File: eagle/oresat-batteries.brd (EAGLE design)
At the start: 94 x 93.5 mm, 73 parts, among them IC1 74AHC1G08DBV, U1 TCAN330, U2 STM32F042K6, U3 ADP5062, X1 16MHz

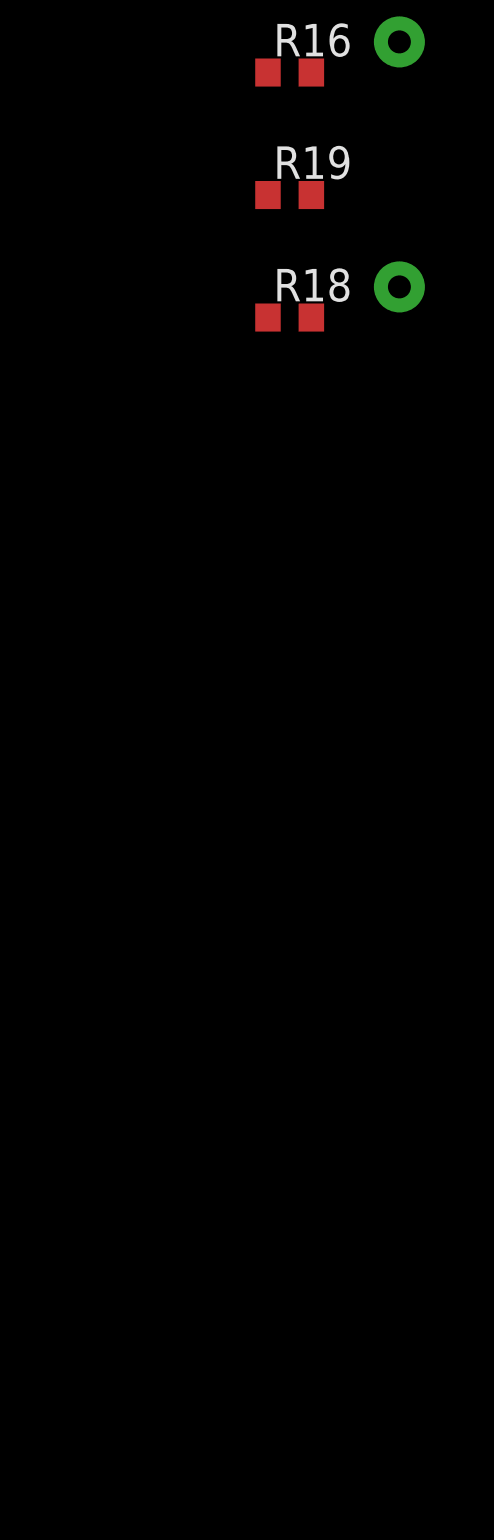
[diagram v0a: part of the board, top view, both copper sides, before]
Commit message: Added 3.3V switching power supply
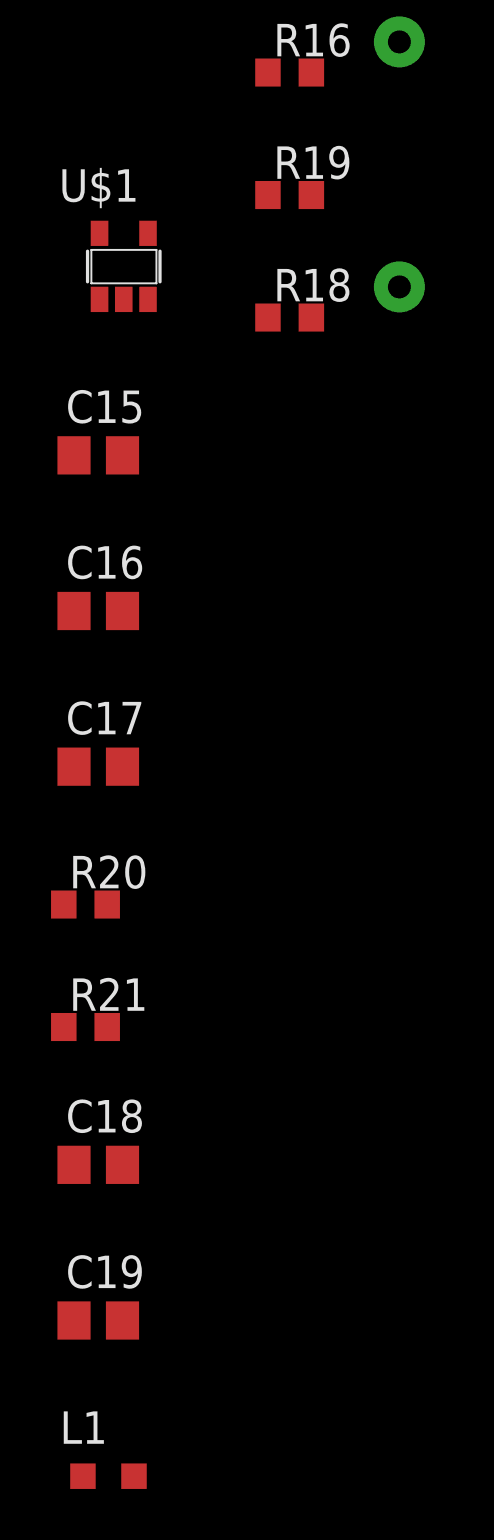
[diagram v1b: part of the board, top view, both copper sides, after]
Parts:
- added C15, C16, C17, C18, C19: 10u, rcl:C0805
- added L1: (no value), rcl:L2012C
- added R20, R21: 10k, rcl:R0603
- added U$1: LM3761, oresat-batteries:SOT23-5
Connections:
- new net N$1: L1.2, U$1.5
- new net N$3: C18.1, C19.1, L1.1, U$1.4
- new net N$7: C17.1, R20.2, R21.1, U$1.3
- net GND: now also C15.2, C16.2, C17.2, C18.2, C19.2, R20.1, U$1.2
- net VSOLAR: now also C15.1, C16.1, R21.2, U$1.1
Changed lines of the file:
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@@
 <element name="R19" library="rcl" package="R0603" value="DNP/10k" x="-21.4" y="-48.5"/>
 <element name="TP5" library="oresat-batteries" package="2MM_TP" value="TP" x="-17.1" y="-52.1"/>
+<element name="U$1" library="oresat-batteries" package="SOT23-5" value="LM3761" x="-27.9" y="-51.3"/>
+<element name="C15" library="rcl" package="C0805" value="10u" x="-28.9" y="-58.7"/>
+<element name="C16" library="rcl" package="C0805" value="10u" x="-28.9" y="-64.8"/>
+<element name="C17" library="rcl" package="C0805" value="10u" x="-28.9" y="-70.9"/>
+<element name="R20" library="rcl" package="R0603" value="10k" x="-29.4" y="-76.3"/>
+<element name="R21" library="rcl" package="R0603" value="10k" x="-29.4" y="-81.1"/>
+<element name="C18" library="rcl" package="C0805" value="10u" x="-28.9" y="-86.5"/>
+<element name="C19" library="rcl" package="C0805" value="10u" x="-28.9" y="-92.6"/>
+<element name="L1" library="rcl" package="L2012C" value="" x="-28.5" y="-98.7"/>
 </elements>
 <signals>
@@
 <contactref element="R17" pad="1"/>
 <contactref element="R19" pad="1"/>
-<wire x1="21.85" y1="80.08" x2="20.85" y2="81.93" width="0" layer="19" extent="1-1"/>
-<wire x1="22.415" y1="75.42" x2="21.85" y2="80.08" width="0" layer="19" extent="1-1"/>
+<contactref element="C16" pad="2"/>
+<contactref element="C15" pad="2"/>
+<contactref element="R20" pad="1"/>
+<contactref element="C19" pad="2"/>
+<contactref element="C18" pad="2"/>
+<contactref element="U$1" pad="2"/>
+<contactref element="C17" pad="2"/>
+<wire x1="-27.95" y1="-86.5" x2="-27.95" y2="-92.6" width="0" layer="19" extent="1-1"/>
+<wire x1="-30.25" y1="-76.3" x2="-27.95" y2="-86.5" width="0" layer="19" extent="1-1"/>
+<wire x1="-27.95" y1="-70.9" x2="-30.25" y2="-76.3" width="0" layer="19" extent="1-1"/>
+<wire x1="-27.95" y1="-64.8" x2="-27.95" y2="-70.9" width="0" layer="19" extent="1-1"/>
+<wire x1="-27.95" y1="-58.7" x2="-27.95" y2="-64.8" width="0" layer="19" extent="1-1"/>
+<wire x1="-27.9" y1="-52.59" x2="-27.95" y2="-58.7" width="0" layer="19" extent="1-1"/>
+<wire x1="-22.25" y1="-48.5" x2="-27.9" y2="-52.59" width="0" layer="19" extent="1-1"/>
+<wire x1="-22.25" y1="-38.9" x2="-22.25" y2="-48.5" width="0" layer="19" extent="1-1"/>
+<wire x1="-22.25" y1="-31.8" x2="-22.25" y2="-38.9" width="0" layer="19" extent="1-1"/>
+<wire x1="-8" y1="-9" x2="-22.25" y2="-31.8" width="0" layer="19" extent="1-1"/>
+<wire x1="-8" y1="-6.5" x2="-8" y2="-9" width="0" layer="19" extent="1-1"/>
+<wire x1="10.39" y1="-13.73" x2="-8" y2="-9" width="0" layer="19" extent="1-1"/>
+<wire x1="10.39" y1="-16.27" x2="10.39" y2="-13.73" width="0" layer="19" extent="1-1"/>
+<wire x1="17.45" y1="14.6" x2="10.39" y2="-13.73" width="0" layer="19" extent="1-1"/>
+<wire x1="19.05" y1="24.91" x2="17.45" y2="14.6" width="0" layer="19" extent="1-1"/>
+<wire x1="24.5" y1="32.5" x2="19.05" y2="24.91" width="0" layer="19" extent="1-1"/>
+<wire x1="24.5" y1="35" x2="24.5" y2="32.5" width="0" layer="19" extent="1-1"/>
+<wire x1="15.15" y1="41.5" x2="24.5" y2="35" width="0" layer="19" extent="1-1"/>
+<wire x1="14.65" y1="52.5" x2="15.15" y2="41.5" width="0" layer="19" extent="1-1"/>
+<wire x1="14.65" y1="56.5" x2="14.65" y2="52.5" width="0" layer="19" extent="1-1"/>
+<wire x1="19.8" y1="58.25" x2="14.65" y2="56.5" width="0" layer="19" extent="1-1"/>
+<wire x1="24.85" y1="61" x2="19.8" y2="58.25" width="0" layer="19" extent="1-1"/>
+<wire x1="24.85" y1="64.5" x2="24.85" y2="61" width="0" layer="19" extent="1-1"/>
+<wire x1="24.85" y1="68.5" x2="24.85" y2="64.5" width="0" layer="19" extent="1-1"/>
+<wire x1="27.175" y1="72.2" x2="24.85" y2="68.5" width="0" layer="19" extent="1-1"/>
+<wire x1="22.415" y1="75.42" x2="27.175" y2="72.2" width="0" layer="19" extent="1-1"/>
+<wire x1="21.85" y1="80.08" x2="22.415" y2="75.42" width="0" layer="19" extent="1-1"/>
+<wire x1="20.85" y1="81.93" x2="21.85" y2="80.08" width="0" layer="19" extent="1-1"/>
 <wire x1="17.325" y1="78.375" x2="21.85" y2="80.08" width="0" layer="19" extent="1-1"/>
 <wire x1="15.675" y1="79.625" x2="17.325" y2="78.375" width="0" layer="19" extent="1-1"/>
@@
 <wire x1="9.35" y1="76" x2="11.65" y2="76" width="0" layer="19" extent="1-1"/>
 <wire x1="7.55" y1="73" x2="9.35" y2="76" width="0" layer="19" extent="1-1"/>
-<wire x1="27.175" y1="72.2" x2="22.415" y2="75.42" width="0" layer="19" extent="1-1"/>
-<wire x1="24.85" y1="68.5" x2="27.175" y2="72.2" width="0" layer="19" extent="1-1"/>
-<wire x1="24.85" y1="64.5" x2="24.85" y2="68.5" width="0" layer="19" extent="1-1"/>
-<wire x1="24.85" y1="61" x2="24.85" y2="64.5" width="0" layer="19" extent="1-1"/>
-<wire x1="19.8" y1="58.25" x2="24.85" y2="61" width="0" layer="19" extent="1-1"/>
-<wire x1="14.65" y1="56.5" x2="19.8" y2="58.25" width="0" layer="19" extent="1-1"/>
-<wire x1="14.65" y1="52.5" x2="14.65" y2="56.5" width="0" layer="19" extent="1-1"/>
 <wire x1="20.95" y1="52.5" x2="19.8" y2="58.25" width="0" layer="19" extent="1-1"/>
 <wire x1="24.85" y1="53" x2="20.95" y2="52.5" width="0" layer="19" extent="1-1"/>
@@
 <wire x1="29.35" y1="57" x2="27.65" y2="53" width="0" layer="19" extent="1-1"/>
 <wire x1="4.25" y1="52.5" x2="14.65" y2="52.5" width="0" layer="19" extent="1-1"/>
-<wire x1="15.15" y1="41.5" x2="14.65" y2="52.5" width="0" layer="19" extent="1-1"/>
-<wire x1="24.5" y1="35" x2="15.15" y2="41.5" width="0" layer="19" extent="1-1"/>
-<wire x1="24.5" y1="32.5" x2="24.5" y2="35" width="0" layer="19" extent="1-1"/>
-<wire x1="19.05" y1="24.91" x2="24.5" y2="32.5" width="0" layer="19" extent="1-1"/>
-<wire x1="17.45" y1="14.6" x2="19.05" y2="24.91" width="0" layer="19" extent="1-1"/>
-<wire x1="32.5" y1="21" x2="24.5" y2="32.5" width="0" layer="19" extent="16-16"/>
-<wire x1="10.39" y1="-13.73" x2="17.45" y2="14.6" width="0" layer="19" extent="1-1"/>
-<wire x1="10.39" y1="-16.27" x2="10.39" y2="-13.73" width="0" layer="19" extent="1-1"/>
-<wire x1="-8" y1="-9" x2="10.39" y2="-13.73" width="0" layer="19" extent="1-1"/>
-<wire x1="-8" y1="-6.5" x2="-8" y2="-9" width="0" layer="19" extent="1-1"/>
-<wire x1="-22.25" y1="-31.8" x2="-8" y2="-9" width="0" layer="19" extent="1-1"/>
-<wire x1="-22.25" y1="-38.9" x2="-22.25" y2="-31.8" width="0" layer="19" extent="1-1"/>
-<wire x1="-22.25" y1="-48.5" x2="-22.25" y2="-38.9" width="0" layer="19" extent="1-1"/>
+<wire x1="32.5" y1="21" x2="19.05" y2="24.91" width="0" layer="19" extent="1-16"/>
 </signal>
 <signal name="ADP_THR">
@@
 <contactref element="R16" pad="2"/>
 <contactref element="R18" pad="2"/>
-<wire x1="20.85" y1="78.23" x2="10.705" y2="92.04" width="0" layer="19" extent="1-1"/>
-<wire x1="21.35" y1="78.23" x2="20.85" y2="78.23" width="0" layer="19" extent="1-1"/>
-<wire x1="21.85" y1="78.23" x2="21.35" y2="78.23" width="0" layer="19" extent="1-1"/>
-<wire x1="34" y1="66.5" x2="21.85" y2="78.23" width="0" layer="19" extent="1-1"/>
-<wire x1="19.05" y1="52.5" x2="34" y2="66.5" width="0" layer="19" extent="1-1"/>
-<wire x1="0.23" y1="-13.73" x2="19.05" y2="52.5" width="0" layer="19" extent="1-1"/>
-<wire x1="0.23" y1="-16.27" x2="0.23" y2="-13.73" width="0" layer="19" extent="1-1"/>
-<wire x1="-20.55" y1="-27" x2="0.23" y2="-16.27" width="0" layer="19" extent="1-1"/>
-<wire x1="-20.55" y1="-43.7" x2="-20.55" y2="-27" width="0" layer="19" extent="1-1"/>
-<wire x1="-20.55" y1="-53.3" x2="-20.55" y2="-43.7" width="0" layer="19" extent="1-1"/>
+<contactref element="U$1" pad="1"/>
+<contactref element="C16" pad="1"/>
+<contactref element="C15" pad="1"/>
+<contactref element="R21" pad="2"/>
+<wire x1="-29.85" y1="-64.8" x2="-28.55" y2="-81.1" width="0" layer="19" extent="1-1"/>
+<wire x1="-29.85" y1="-58.7" x2="-29.85" y2="-64.8" width="0" layer="19" extent="1-1"/>
+<wire x1="-28.85" y1="-52.59" x2="-29.85" y2="-58.7" width="0" layer="19" extent="1-1"/>
+<wire x1="-20.55" y1="-53.3" x2="-28.85" y2="-52.59" width="0" layer="19" extent="1-1"/>
+<wire x1="-20.55" y1="-43.7" x2="-20.55" y2="-53.3" width="0" layer="19" extent="1-1"/>
+<wire x1="-20.55" y1="-27" x2="-20.55" y2="-43.7" width="0" layer="19" extent="1-1"/>
+<wire x1="0.23" y1="-16.27" x2="-20.55" y2="-27" width="0" layer="19" extent="1-1"/>
+<wire x1="0.23" y1="-13.73" x2="0.23" y2="-16.27" width="0" layer="19" extent="1-1"/>
+<wire x1="19.05" y1="52.5" x2="0.23" y2="-13.73" width="0" layer="19" extent="1-1"/>
+<wire x1="34" y1="66.5" x2="19.05" y2="52.5" width="0" layer="19" extent="1-1"/>
+<wire x1="21.85" y1="78.23" x2="34" y2="66.5" width="0" layer="19" extent="1-1"/>
+<wire x1="21.35" y1="78.23" x2="21.85" y2="78.23" width="0" layer="19" extent="1-1"/>
+<wire x1="20.85" y1="78.23" x2="21.35" y2="78.23" width="0" layer="19" extent="1-1"/>
+<wire x1="10.705" y1="92.04" x2="20.85" y2="78.23" width="0" layer="19" extent="1-1"/>
 </signal>
 <signal name="ADP_CBP">
@@
 <wire x1="-21.5" y1="-19.11" x2="-21.175" y2="-18.065" width="0" layer="19" extent="1-1"/>
 </signal>
+<signal name="N$1">
+<contactref element="U$1" pad="5"/>
+<contactref element="L1" pad="2"/>
+<wire x1="-28.85" y1="-50" x2="-27.5" y2="-98.7" width="0" layer="19" extent="1-1"/>
+</signal>
+<signal name="N$3">
+<contactref element="U$1" pad="4"/>
+<contactref element="L1" pad="1"/>
+<contactref element="C19" pad="1"/>
+<contactref element="C18" pad="1"/>
+<wire x1="-29.85" y1="-92.6" x2="-29.5" y2="-98.7" width="0" layer="19" extent="1-1"/>
+<wire x1="-29.85" y1="-86.5" x2="-29.85" y2="-92.6" width="0" layer="19" extent="1-1"/>
+<wire x1="-26.95" y1="-50" x2="-29.85" y2="-86.5" width="0" layer="19" extent="1-1"/>
+</signal>
+<signal name="N$7">
+<contactref element="R21" pad="1"/>
+<contactref element="R20" pad="2"/>
+<contactref element="C17" pad="1"/>
+<contactref element="U$1" pad="3"/>
+<wire x1="-28.55" y1="-76.3" x2="-30.25" y2="-81.1" width="0" layer="19" extent="1-1"/>
+<wire x1="-29.85" y1="-70.9" x2="-28.55" y2="-76.3" width="0" layer="19" extent="1-1"/>
+<wire x1="-26.95" y1="-52.59" x2="-29.85" y2="-70.9" width="0" layer="19" extent="1-1"/>
+</signal>
 </signals>
